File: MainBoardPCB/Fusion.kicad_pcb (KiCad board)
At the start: 4 copper layers, 91.5 x 52.1 mm, 140 parts, among them J1 Micro_SD_Card_Det_Hirose_DM3AT, J2 Conn_02x20_Odd_Even, J3 DX07S016JA1R1500, J4 Conn_02x07_Odd_Even, J5 Conn_02x16_Odd_Even, J7 Conn_02x08_Odd_Even, SW1 SW_Push, SW2 SW_Push, SW3 RESET, SW4 BOOT0, U1 STM32F723IETx, U2 TLV62568DDC, U3 MX25L3233FM1, U4 LFE5U-12-TG144, U5 NCP718xSN250, U6 USB6B1, U8 UGA, U9 TLV62568DDC, Y1 12MHz

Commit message: Fixes mistake in 1.0, FPGA boot cgf was forced into Master SPI mode
Just make it configurable with pull down resistors.

Signed-off-by: Alexis Jeandet <alexis.jeandet@member.fsf.org>
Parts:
- removed C55: 100nF, Capacitor_SMD:C_0402_1005Metric
- added R42: R, Resistor_SMD:R_0402_1005Metric_Pad0.72x0.64mm_HandSolder, B.Cu at (129.1, 79.7)
- added R43: R, Resistor_SMD:R_0402_1005Metric_Pad0.72x0.64mm_HandSolder, B.Cu at (130.2, 79.7)
- added R44: R, Resistor_SMD:R_0402_1005Metric_Pad0.72x0.64mm_HandSolder, B.Cu at (131.4, 79.7)
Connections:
- U4 pad 58: GND -> /FPGA/CFG_2
- U4 pad 59: /#3.3V -> /FPGA/CFG_1
- U4 pad 62: GND -> /FPGA/CFG_0
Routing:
- net /FPGA/CFG_2: track 0.00 -> 8.80 mm, vias 0 -> 1
- net /FPGA/CFG_1: track 0.00 -> 7.39 mm, vias 0 -> 1
- net /FPGA/CFG_0: track 0.00 -> 6.17 mm, vias 0 -> 1
- net /#3.3V: track 132.8 -> 130.9 mm, vias 42 -> 41
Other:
- board text added: "CFG0"
- board text added: "CFG1"
- board text added: "CFG2"

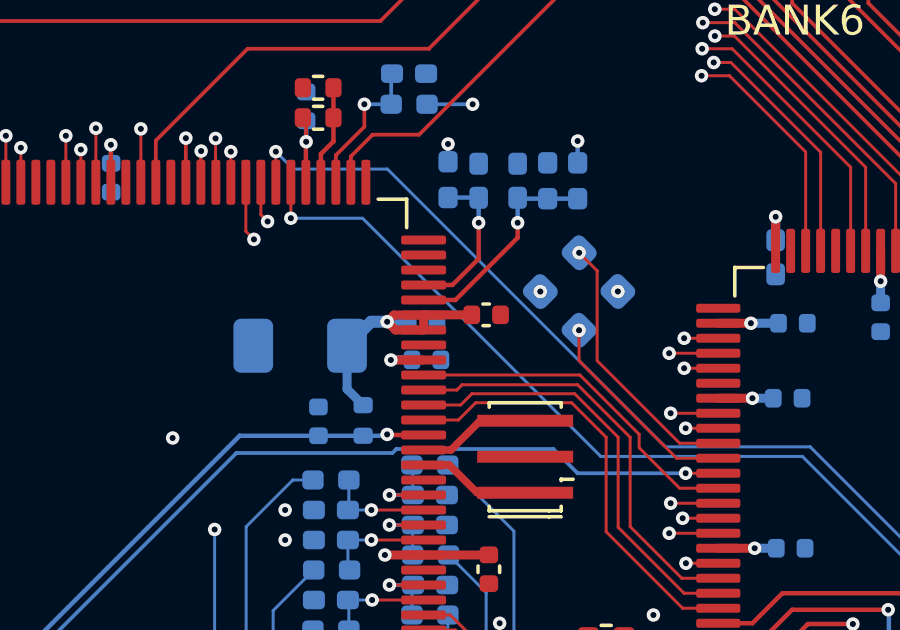
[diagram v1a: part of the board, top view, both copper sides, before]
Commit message: Fixes FPGA CFG slave serial interface wiring
Signed-off-by: Alexis Jeandet <alexis.jeandet@member.fsf.org>
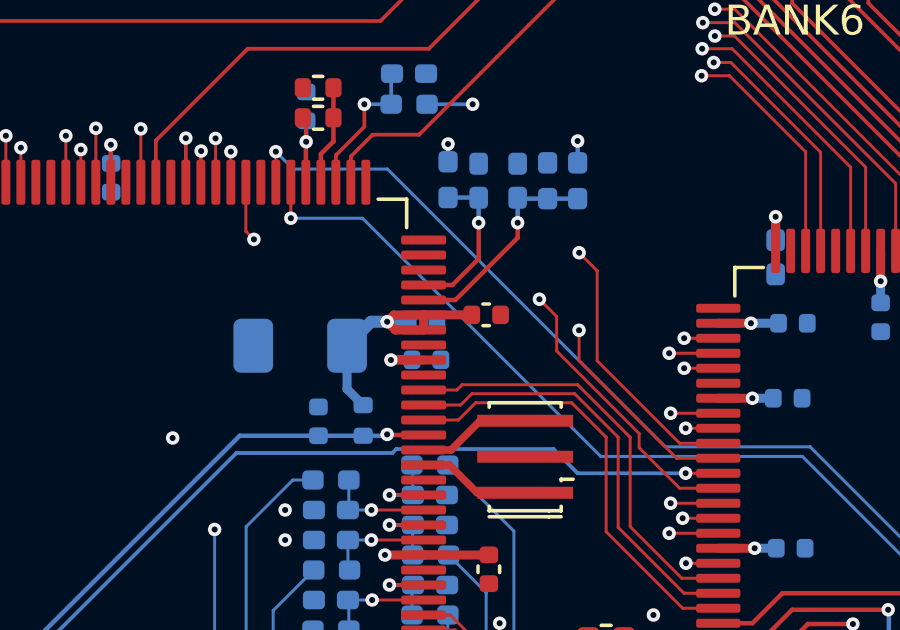
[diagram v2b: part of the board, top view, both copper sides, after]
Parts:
- removed U8: UGA, UGA:UGA_0603
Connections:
- U1 pad 35: /FPGA/FPGA_CFG_HOLDN -> /MCU/FPGA_CFG_HOLDN
- U1 pad 52: /FPGA/FPGA_CFG_MISO -> unconnected-(U1-PA6-Pad52)
- U4 pad 46: Net-(U4G-PB11A/+/D1/MISO/IO1) -> unconnected-(U4G-PB11A/+/D1/MISO/IO1-Pad46)
- U4 pad 47: Net-(U4G-PB11B/-/D0/MOSI/IO0) -> unconnected-(U4G-PB11B/-/D0/MOSI/IO0-Pad47)
- U4 pad 49: /FPGA/FPGA_CFG_HOLDN -> /FPGA/FPGA_CFG_MOSI
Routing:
- net /FPGA/FPGA_CFG_MISO: track 14.0 -> 0.00 mm, vias 2 -> 0
- net /FPGA/FPGA_CFG_HOLDN: track 11.6 -> 0.00 mm
- net /FPGA/FPGA_CFG_MOSI: track 12.3 -> 21.9 mm
- net unconnected-(U4G-PB11A/+/D1/MISO/IO1-Pad46): track 0.00 -> 9.03 mm, vias 0 -> 1
- net Net-(U4G-PB11A/+/D1/MISO/IO1): track 9.03 -> 0.00 mm, vias 1 -> 0
- net unconnected-(U4G-PB11B/-/D0/MOSI/IO0-Pad47): track 0.00 -> 7.00 mm, vias 0 -> 1
- net Net-(U4G-PB11B/-/D0/MOSI/IO0): track 7.00 -> 0.00 mm, vias 1 -> 0

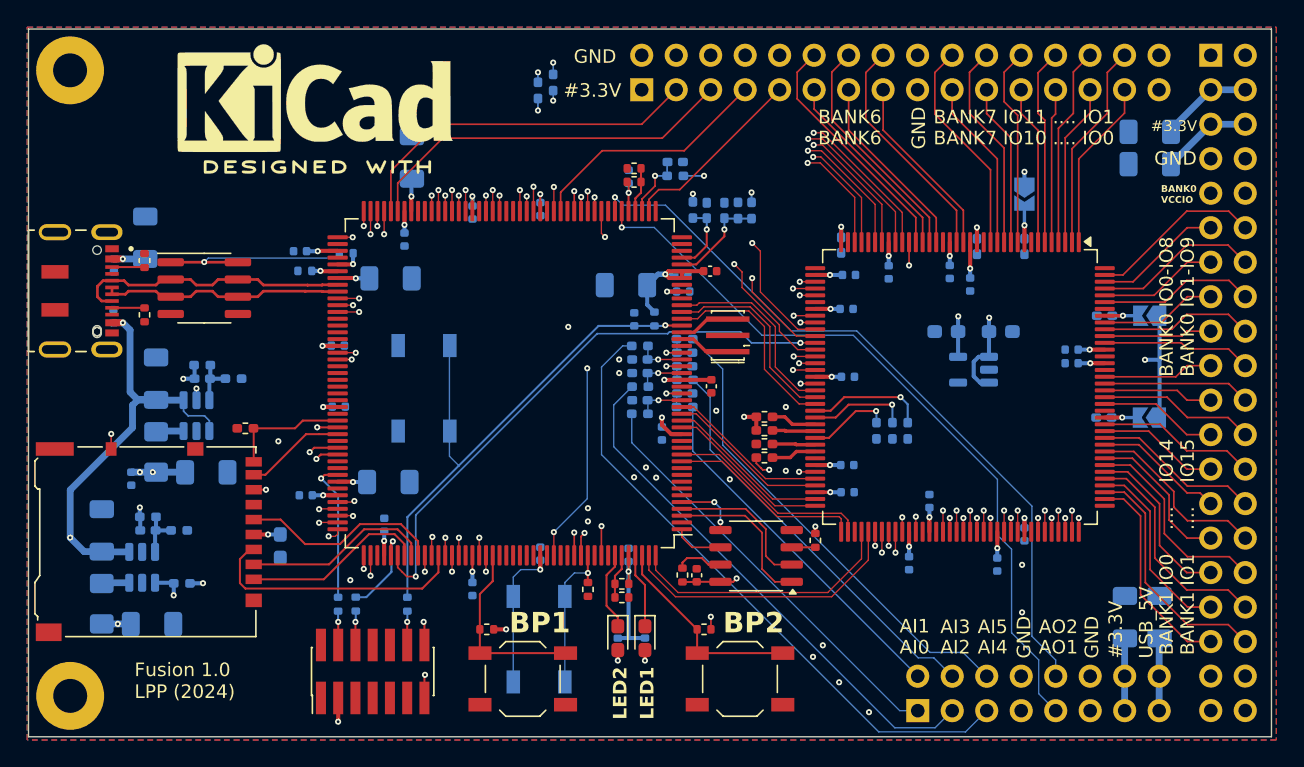
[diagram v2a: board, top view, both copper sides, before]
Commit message: New Fusion main board version using a more beefy MCU.
Signed-off-by: Alexis Jeandet <alexis.jeandet@member.fsf.org>
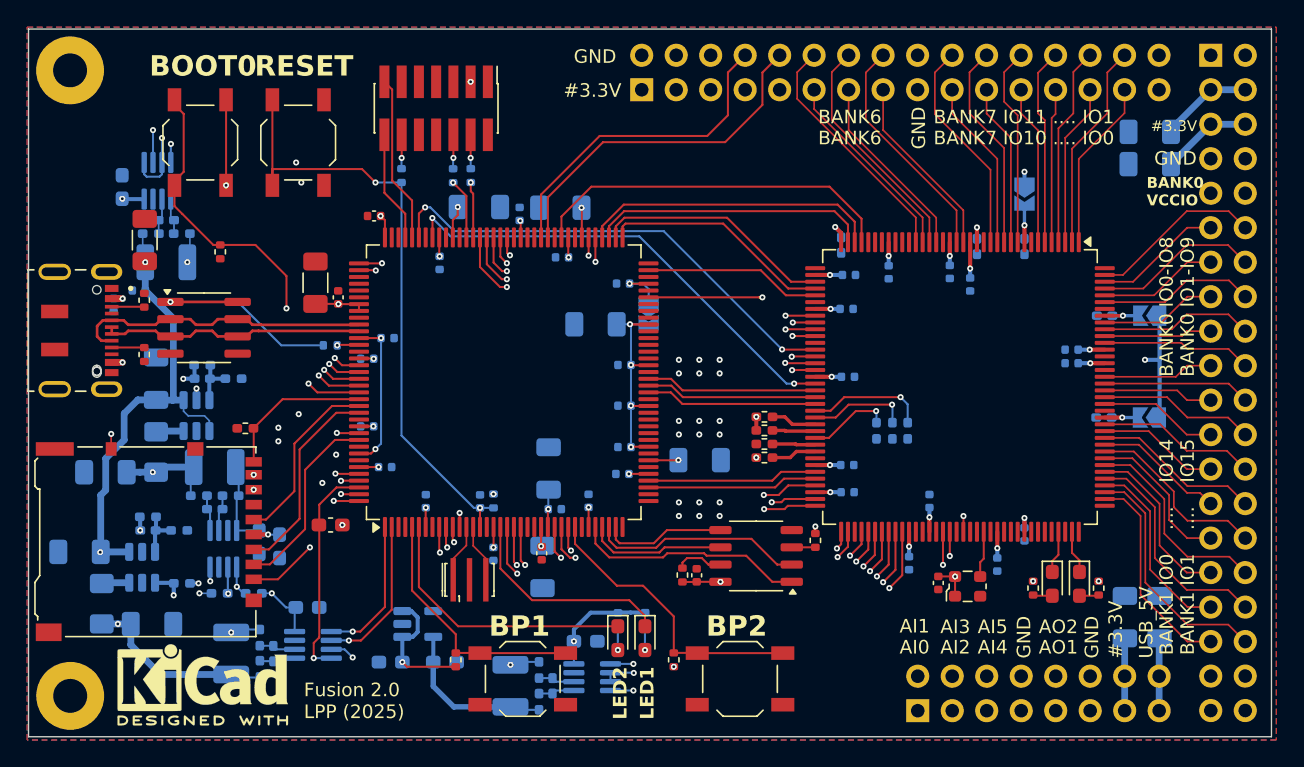
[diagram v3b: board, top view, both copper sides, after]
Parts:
- removed C13, C24, C25, C28, C29, C7: 100nF, Capacitor_SMD:C_0402_1005Metric
- removed C2, C21: 2.2µF, Capacitor_SMD:C_1206_3216Metric_Pad1.33x1.80mm_HandSolder
- removed C37, C41, C42, C43, C44, C45: 10nF, Capacitor_SMD:C_0402_1005Metric_Pad0.74x0.62mm_HandSolder
- removed C47, C48, C69: 100nF, Capacitor_SMD:C_0402_1005Metric_Pad0.74x0.62mm_HandSolder
- removed R10: 3K, Resistor_SMD:R_0402_1005Metric
- removed R15, R21, R22, R23, R24, R25: 1k, Resistor_SMD:R_0402_1005Metric_Pad0.72x0.64mm_HandSolder
- removed R19: 10k, Resistor_SMD:R_0402_1005Metric
- removed R35, R36, R37, R41: 10k, Resistor_SMD:R_0402_1005Metric_Pad0.72x0.64mm_HandSolder
- removed R5, R6, R7: 100k, Resistor_SMD:R_0402_1005Metric
- removed SYM1: Logo_Open_Hardware_Small, Symbol:OSHW-Logo_11.4x12mm_SilkScreen
- removed SYM2: Logo_Open_Hardware_Small, Symbol:KiCad-Logo2_8mm_SilkScreen
- removed U1: STM32F723IETx, Package_QFP:LQFP-176_24x24mm_P0.5mm
- added C1: 100nF, Capacitor_SMD:C_0402_1005Metric, F.Cu at (133.6, 90.9)
- added C1001: 100nF, Capacitor_SMD:C_0402_1005Metric_Pad0.74x0.62mm_HandSolder, B.Cu at (76.7, 64.2)
- added C1002: 100nF, Capacitor_SMD:C_0603_1608Metric_Pad1.08x0.95mm_HandSolder, B.Cu at (73.5, 61.8)
- added C217: 1µF, Capacitor_SMD:C_1206_3216Metric_Pad1.33x1.80mm_HandSolder, B.Cu at (104.5, 89.8)
- added C219: 100nF, Capacitor_SMD:C_0402_1005Metric, F.Cu at (104.4, 88.7)
- added C220: 100nF, Capacitor_SMD:C_0402_1005Metric, B.Cu at (93.0, 72.9)
- added C222: 2.2µF, Capacitor_SMD:C_1206_3216Metric_Pad1.33x1.80mm_HandSolder, B.Cu at (116.0, 81.9)
- added C223: 1µF, Capacitor_SMD:C_1206_3216Metric_Pad1.33x1.80mm_HandSolder, B.Cu at (104.9, 82.5)
- added C224: 100nF, Capacitor_SMD:C_0402_1005Metric, B.Cu at (105.4, 85.5)
- added C225: 1µF, Capacitor_SMD:C_1206_3216Metric_Pad1.33x1.80mm_HandSolder, F.Cu at (87.7, 68.8)
- added C226: 100nF, Capacitor_SMD:C_0402_1005Metric, F.Cu at (89.4, 69.9)
- added C227: 1µF, Capacitor_SMD:C_1206_3216Metric_Pad1.33x1.80mm_HandSolder, B.Cu at (108.4, 71.9)
- added C228: 100nF, Capacitor_SMD:C_0402_1005Metric, B.Cu at (110.5, 80.9)
- added C229: 100nF, Capacitor_SMD:C_0402_1005Metric, B.Cu at (110.5, 77.9)
- added C230: 100nF, Capacitor_SMD:C_0402_1005Metric, B.Cu at (110.5, 74.9)
- added C501: 100nF, Capacitor_SMD:C_0402_1005Metric_Pad0.74x0.62mm_HandSolder, B.Cu at (80.3, 85.5)
- added C502: 100nF, Capacitor_SMD:C_0603_1608Metric_Pad1.08x0.95mm_HandSolder, B.Cu at (83.6, 87.9)
- added C801: 100nF, Capacitor_SMD:C_0402_1005Metric_Pad0.74x0.62mm_HandSolder, B.Cu at (84.6, 96.1)
- added C802: 100nF, Capacitor_SMD:C_0603_1608Metric_Pad1.08x0.95mm_HandSolder, B.Cu at (87.1, 92.7)
- added C901: 100nF, Capacitor_SMD:C_0402_1005Metric_Pad0.74x0.62mm_HandSolder, B.Cu at (105.2, 98.5)
- added C902: 100nF, Capacitor_SMD:C_0603_1608Metric_Pad1.08x0.95mm_HandSolder, B.Cu at (107.6, 95.2)
- added D301: LED, LED_SMD:LED_0603_1608Metric_Pad1.05x0.95mm_HandSolder, F.Cu at (142.0, 91.0)
- added D302: LED, LED_SMD:LED_0603_1608Metric_Pad1.05x0.95mm_HandSolder, F.Cu at (144.0, 91.0)
- added JP201: SolderJumper_2_Open, Jumper:SolderJumper-2_P1.3mm_Open_TrianglePad1.0x1.5mm, B.Cu at (112.3, 71.1)
- added R1001: R, Resistor_SMD:R_1210_3225Metric_Pad1.30x2.65mm_HandSolder, B.Cu at (76.7, 67.3)
- added R1002: 100, Resistor_SMD:R_0402_1005Metric_Pad0.72x0.64mm_HandSolder, B.Cu at (77.9, 65.2)
- added R1003: 100, Resistor_SMD:R_0402_1005Metric_Pad0.72x0.64mm_HandSolder, B.Cu at (75.6, 65.2)
- added R101: 10k, Capacitor_SMD:C_0603_1608Metric_Pad1.08x0.95mm_HandSolder, F.Cu at (88.8, 86.7)
- added R308: 2.2k, Resistor_SMD:R_0402_1005Metric, F.Cu at (140.6, 91.3)
- added R309: 2.2k, Resistor_SMD:R_0402_1005Metric, F.Cu at (145.4, 91.3)
- added R501: R, Resistor_SMD:R_1210_3225Metric_Pad1.30x2.65mm_HandSolder, B.Cu at (80.3, 82.4)
- added R502: 100, Resistor_SMD:R_0402_1005Metric_Pad0.72x0.64mm_HandSolder, B.Cu at (79.1, 84.5)
- added R503: 100, Resistor_SMD:R_0402_1005Metric_Pad0.72x0.64mm_HandSolder, B.Cu at (81.5, 84.5)
- added R801: R, Resistor_SMD:R_1210_3225Metric_Pad1.30x2.65mm_HandSolder, B.Cu at (81.5, 96.1)
- added R802: 100, Resistor_SMD:R_0402_1005Metric_Pad0.72x0.64mm_HandSolder, B.Cu at (83.6, 97.3)
- added R803: 100, Resistor_SMD:R_0402_1005Metric_Pad0.72x0.64mm_HandSolder, B.Cu at (83.6, 95.0)
- added R901: R, Resistor_SMD:R_1210_3225Metric_Pad1.30x2.65mm_HandSolder, B.Cu at (102.1, 98.5)
- added R902: 100, Resistor_SMD:R_0402_1005Metric_Pad0.72x0.64mm_HandSolder, B.Cu at (104.2, 99.7)
- added R903: 100, Resistor_SMD:R_0402_1005Metric_Pad0.72x0.64mm_HandSolder, B.Cu at (104.2, 97.3)
- added REF**: KiCad-Logo2_5mm_SilkScreen, Symbol:KiCad-Logo2_5mm_SilkScreen, F.Cu at (79.4, 98.4)
- added SYM101: Logo_Open_Hardware_Small, Symbol:OSHW-Logo_11.4x12mm_SilkScreen, B.Cu at (120.6, 95.4)
- added U1001: INA236, Package_TO_SOT_SMD:SOT-23-8_Handsoldering, B.Cu at (76.1, 61.3)
- added U203: STM32H7S3Z8Tx, Package_QFP:LQFP-144_20x20mm_P0.5mm, F.Cu at (101.6, 76.1)
- added U501: INA236, Package_TO_SOT_SMD:SOT-23-8_Handsoldering, B.Cu at (80.9, 88.4)
- added U801: INA236, Package_TO_SOT_SMD:SOT-23-8_Handsoldering, B.Cu at (87.5, 95.5)
- added U901: INA236, Package_TO_SOT_SMD:SOT-23-8_Handsoldering, B.Cu at (108.1, 97.9)
- added X1: ECS-2520MV-xxx-xx, Oscillator:Oscillator_SMD_ECS_2520MV-xxx-xx-4Pin_2.5x2.0mm, F.Cu at (135.8, 91.2)
- C207: renamed from C15; moved to B.Cu
- C211: renamed from C17; moved to F.Cu
- C402: renamed from C8; value 10µF -> 100nF; footprint Capacitor_SMD:C_1206_3216Metric_Pad1.33x1.80mm_HandSolder -> Capacitor_SMD:C_0402_1005Metric
- C403: renamed from C10; value 100nF -> 10µF; footprint Capacitor_SMD:C_0402_1005Metric -> Capacitor_SMD:C_1206_3216Metric_Pad1.33x1.80mm_HandSolder; moved to F.Cu
- SW203: renamed from SW4; moved to F.Cu
- SW204: renamed from SW3; moved to F.Cu
- moved C401 51.1 mm to (93.3, 96.8), turned to 180 degrees
- moved U401 45.0 mm to (95.3, 94.0), turned to 0 degrees
- moved SW203 44.3 mm to (79.2, 58.5)
- moved C404 44.2 mm to (97.3, 96.8), turned to 0 degrees
- moved R216 43.8 mm to (80.7, 91.7), turned to 180 degrees
- moved R217 43.6 mm to (83.2, 91.7), turned to 0 degrees
- moved J201 41.7 mm to (96.6, 56.0), turned to -90 degrees
- moved R215 36.8 mm to (80.7, 66.5)
- moved C212 33.7 mm to (107.8, 84.9), turned to 90 degrees
- moved R203 33.0 mm to (99.2, 60.9), turned to -90 degrees
- moved R204 32.4 mm to (97.9, 60.9), turned to -90 degrees
- moved R205 31.6 mm to (94.1, 60.9), turned to -90 degrees
- moved C211 27.7 mm to (92.0, 63.9), turned to 180 degrees
- moved C208 26.4 mm to (102.8, 63.8)
- moved Y201 26.2 mm to (99.1, 90.7), turned to 0 degrees
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- renumbered C49 to C101, C19 to C102, C50 to C103, C20 to C104, C3 to C201, C4 to C202, C51 to C203, C26 to C204, C27 to C205, C9 to C206, C16 to C208, C11 to C209, C12 to C210, C22 to C212, C30 to C213, C1 to C214, C46 to C215, C14 to C216, C18 to C218, C23 to C221, C65 to C301, C66 to C302, C67 to C303, C68 to C304, C59 to C305, C60 to C306, C61 to C307, C62 to C308, C5 to C309, C63 to C310, C64 to C311, C31 to C312, C54 to C313, C33 to C314, C56 to C315, C57 to C316, C35 to C317, C58 to C318, C36 to C319, C52 to C401, C53 to C404, C6 to C601, C32 to C602, C34 to C603, C38 to C701, C39 to C702, C40 to C703, D1 to D201, D2 to D202, H1 to H101, H2 to H102, J7 to J101, J5 to J102, J2 to J103, J4 to J201, J1 to J202, J3 to J203, JP1 to JP101, JP2 to JP102, JP3 to JP103, L2 to L601, L3 to L701, R16 to R201, R4 to R202, R1 to R203, R2 to R204, R3 to R205, R14 to R206, R20 to R207, R38 to R208, R12 to R209, R13 to R210, R17 to R211, R18 to R212, R11 to R213, R8 to R214, R9 to R215, R39 to R216, R40 to R217, R26 to R301, R27 to R302, R28 to R303, R29 to R304, R42 to R305, R43 to R306, R44 to R307, R34 to R401, R31 to R601, R32 to R602, R30 to R701, R33 to R702, SW1 to SW201, SW2 to SW202, U3 to U201, U6 to U202, U4 to U301, U5 to U401, U2 to U601, U9 to U701, Y1 to Y201
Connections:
- C103 pad 1: /USB_5V -> /5V
- C104 pad 1: /USB_5V -> /5V
- C218 pad 1: Net-(U1-V12PHYHS) -> /MCU/VCap
- C221 pad 1: /#3.3V -> /MCU/VCap
- C402 pad 1: /USB_5V -> /5V
- C403 pad 1: /USB_5V -> /5V
- C404 pad 1: /#2.5V -> /Power/PowerMonitor2/Vin
- C601 pad 1: /USB_5V -> /5V
- C602 pad 1: /#3.3V -> /Power/PowerMonitor1/Vin
- C603 pad 1: /#3.3V -> /Power/PowerMonitor1/Vin
- C701 pad 1: /USB_5V -> /5V
- C702 pad 1: /#1.1V -> /Power/PowerMonitor/Vin
- C703 pad 1: /#1.1V -> /Power/PowerMonitor/Vin
- J101 pad 15: /USB_5V -> /5V
- J101 pad 16: /USB_5V -> /5V
- J103 pad 3: /USB_5V -> /5V
- J103 pad 4: /USB_5V -> /5V
- L601 pad 2: /#3.3V -> /Power/PowerMonitor1/Vin
- L701 pad 2: /#1.1V -> /Power/PowerMonitor/Vin
- R213 pad 1: Net-(U1-PB13) -> /MCU/VBUS_SENSE
- R601 pad 1: /#3.3V -> /Power/PowerMonitor1/Vin
- R701 pad 1: /#1.1V -> /Power/PowerMonitor/Vin
- U301 pad 102: /FPGA/FPGA_D13 -> unconnected-(U301C-PR8D/-/RDQ8-Pad102)
- U301 pad 103: /FPGA/FPGA_D20 -> unconnected-(U301C-PR8B/-/HS/RDQSN8-Pad103)
- U301 pad 104: /FPGA/FPGA_D19 -> unconnected-(U301C-PR8C/+/RDQ8-Pad104)
- U301 pad 105: /FPGA/FPGA_D18 -> /FPGA/LED1
- U301 pad 106: /FPGA/FPGA_D17 -> unconnected-(U301C-PR2D/-/RDQ8-Pad106)
- U301 pad 107: /FPGA/FPGA_D16 -> /FPGA/LED2
- U301 pad 108: /FPGA/FPGA_D12 -> unconnected-(U301C-PR2B/-/HS/RDQ8/S0_IN-Pad108)
- U301 pad 26: /FPGA/FPGA_NL -> unconnected-(U301E-PL41C/+/LDQ44-Pad26)
- U301 pad 27: /FPGA/FPGA_IO5 -> unconnected-(U301E-PL41D/-/LDQ44-Pad27)
- U301 pad 28: /FPGA/FPGA_IO4 -> unconnected-(U301E-PL44A/+/HS/LDQS44-Pad28)
- U301 pad 30: /FPGA/FPGA_IO3 -> unconnected-(U301E-PL44B/-/HS/LDQSN44-Pad30)
- U301 pad 31: /FPGA/FPGA_IO2 -> unconnected-(U301E-PL44C/+/LDQ44-Pad31)
- U301 pad 33: /FPGA/FPGA_IO1 -> /FPGA/FPGA_HAVE_DATA
- U301 pad 34: /FPGA/FPGA_IO0 -> /FPGA/FPGA_D8
- U301 pad 35: unconnected-(U4E-PL47B/-/HS/LDQ44-Pad35) -> /FPGA/FPGA_D9
- U301 pad 39: /FPGA/FPGA_D4 -> /FPGA/FPGA_D10
- U301 pad 40: /FPGA/FPGA_D5 -> /FPGA/FPGA_D11
- U301 pad 41: /FPGA/FPGA_D6 -> /FPGA/FPGA_NE1
- U301 pad 44: /FPGA/FPGA_D7 -> /FPGA/FPGA_D4
- U301 pad 45: /FPGA/FPGA_D8 -> /FPGA/FPGA_D3
- U301 pad 46: unconnected-(U4G-PB11A/+/D1/MISO/IO1-Pad46) -> /FPGA/FPGA_D2
- U301 pad 47: unconnected-(U4G-PB11B/-/D0/MOSI/IO0-Pad47) -> /FPGA/FPGA_D1
- U301 pad 48: /FPGA/FPGA_CFG_CS -> unconnected-(U301G-PB13A/+/SN/CSN-Pad48)
- U301 pad 50: /FPGA/FPGA_D9 -> /FPGA/FPGA_D0
- U301 pad 51: /FPGA/FPGA_D10 -> /FPGA/FPGA_NWAIT
- U301 pad 52: /FPGA/FPGA_D11 -> /FPGA/FPGA_NL
- U301 pad 67: /FPGA/FPGA_NWAIT -> /FPGA/FPGA_NWE
- U301 pad 68: /FPGA/FPGA_HAVE_DATA -> /FPGA/FPGA_NOE
- U301 pad 69: /FPGA/FPGA_A2 -> /FPGA/FPGA_D5
- U301 pad 71: /FPGA/FPGA_A1 -> /FPGA/FPGA_D6
- U301 pad 72: /FPGA/FPGA_A0 -> /FPGA/FPGA_D7
- U301 pad 73: /FPGA/FPGA_D30 -> /FPGA/FPGA_A2
- U301 pad 74: /FPGA/FPGA_D31 -> /FPGA/FPGA_A1
- U301 pad 76: /FPGA/FPGA_D29 -> /FPGA/FPGA_A0
- U301 pad 77: /FPGA/FPGA_D28 -> /FPGA/FPGA_D15
- U301 pad 78: /FPGA/FPGA_D26 -> /FPGA/FPGA_D14
- U301 pad 79: /FPGA/FPGA_D27 -> /FPGA/FPGA_D13
- U301 pad 80: /FPGA/FPGA_D25 -> /FPGA/FPGA_D12
- U301 pad 81: /FPGA/FPGA_D24 -> /FPGA/FPGA_UART_TX
- U301 pad 82: /FPGA/FPGA_D23 -> /FPGA/FPGA_UART_RX
- U301 pad 84: /FPGA/FPGA_D22 -> unconnected-(U301D-PR32C/+/RDQ32-Pad84)
- U301 pad 88: /FPGA/FPGA_D21 -> /FPGA/FPGA_UART2_RX
- U301 pad 89: /FPGA/FPGA_NE1 -> /FPGA/FPGA_UART2_TX
- U301 pad 90: /FPGA/FPGA_NOE -> unconnected-(U301C-PR23C/+/RDQ20/PCLKT2_0-Pad90)
- U301 pad 91: /FPGA/FPGA_D2 -> /FPGA/FPGA_CLK
- U301 pad 92: /FPGA/FPGA_D3 -> unconnected-(U301C-PR20D/-/RDQ20-Pad92)
- U301 pad 93: /FPGA/FPGA_CLK -> unconnected-(U301C-PR20B/-/HS/RDQSN20-Pad93)
- U301 pad 94: /FPGA/FPGA_NWE -> /FPGA/FPGA_OPT_CLK
- U301 pad 95: /FPGA/FPGA_D1 -> unconnected-(U301C-PR20A/+/HS/RDQS20/GR_PCLK2_1-Pad95)
- U301 pad 97: /FPGA/FPGA_D0 -> unconnected-(U301C-PR14B/-/HS/RDQ20-Pad97)
- U301 pad 98: /FPGA/FPGA_D15 -> unconnected-(U301C-PR14C/+/RDQ20/VREF1_2-Pad98)
- U301 pad 99: /FPGA/FPGA_D14 -> unconnected-(U301C-PR14A/+/HS/RDQ20-Pad99)
- U401 pad 5: /#2.5V -> /Power/PowerMonitor2/Vin
- U601 pad 1: /USB_5V -> /5V
- U601 pad 4: /USB_5V -> /5V
- U701 pad 4: /USB_5V -> /5V
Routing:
- net /5V: track 0.00 -> 181.1 mm, vias 0 -> 2
- net /USB_5V: track 211.2 -> 34.4 mm
- net /Alert: track 0.00 -> 88.7 mm, vias 0 -> 4
- net /FPGA/FPGA_D18: track 63.0 -> 0.00 mm, vias 2 -> 0
- net /FPGA/FPGA_D17: track 63.0 -> 0.00 mm, vias 2 -> 0
- net /FPGA/FPGA_D16: track 63.0 -> 0.00 mm, vias 2 -> 0
- net /FPGA/FPGA_D19: track 63.0 -> 0.00 mm, vias 2 -> 0
- net /FPGA/FPGA_D20: track 62.2 -> 0.00 mm, vias 2 -> 0
- net /MCU/VCap: track 0.00 -> 61.9 mm, vias 0 -> 5
- net /FPGA/FPGA_UART2_TX: track 0.00 -> 57.2 mm, vias 0 -> 2
- net /FPGA/FPGA_UART2_RX: track 0.00 -> 55.4 mm, vias 0 -> 2
- net /DAC_OUT1: track 55.4 -> 0.00 mm, vias 1 -> 0
- net /DAC_OUT2: track 54.4 -> 0.00 mm, vias 1 -> 0
- net /FPGA/FPGA_D22: track 52.7 -> 0.00 mm, vias 2 -> 0
- net /FPGA/FPGA_UART_TX: track 0.00 -> 52.7 mm, vias 0 -> 2
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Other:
- board text added: "Fusion 2.0 LPP (2025)"
- board text removed: "Fusion 1.0 LPP (2024)"

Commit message: New FPGA only version
Signed-off-by: Alexis Jeandet <alexis.jeandet@member.fsf.org>
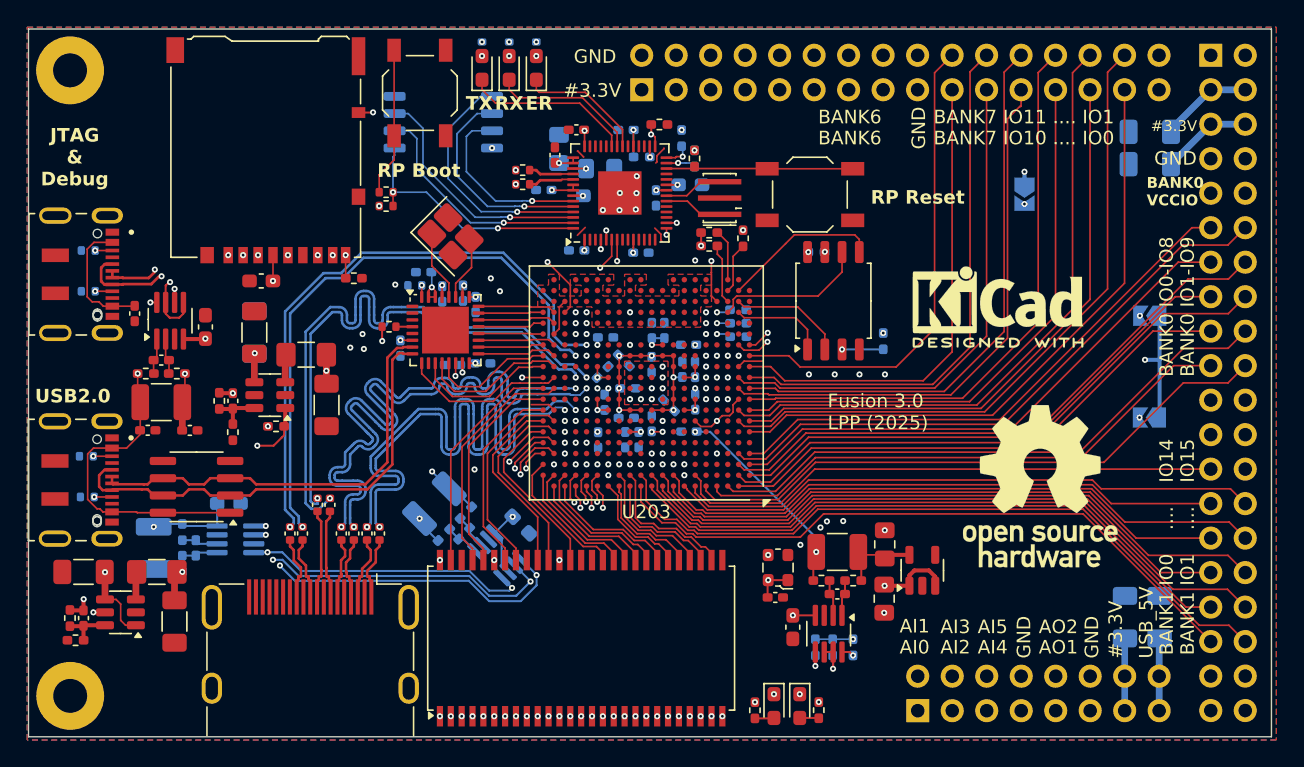
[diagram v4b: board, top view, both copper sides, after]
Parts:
- removed C209, C210, C211, C212, C213, C216, C219, C220, C224, C226, C228, C229, C230: 100nF, Capacitor_SMD:C_0402_1005Metric
- removed C214: 100nF, Capacitor_SMD:C_0603_1608Metric_Pad1.08x0.95mm_HandSolder
- removed C217, C223, C225, C227: 1µF, Capacitor_SMD:C_1206_3216Metric_Pad1.33x1.80mm_HandSolder
- removed C218, C221, C222: 2.2µF, Capacitor_SMD:C_1206_3216Metric_Pad1.33x1.80mm_HandSolder
- removed D201, D202: LED, LED_SMD:LED_0603_1608Metric_Pad1.05x0.95mm_HandSolder
- removed JP201: SolderJumper_2_Open, Jumper:SolderJumper-2_P1.3mm_Open_TrianglePad1.0x1.5mm
- removed R206, R214, R215: 100k, Resistor_SMD:R_0402_1005Metric
- removed R207, R208, R209, R210: 2.2k, Resistor_SMD:R_0402_1005Metric
- removed R216, R217: 10k, Resistor_SMD:R_0402_1005Metric_Pad0.72x0.64mm_HandSolder
- removed SW202: SW_Push, Button_Switch_SMD:SW_SPST_TL3342
- removed SW203: BOOT0, Button_Switch_SMD:SW_SPST_TL3342
- removed SW204: RESET, Button_Switch_SMD:SW_SPST_TL3342
- removed U201: MX25L3233FM1, Package_SO:SOP-8_3.9x4.9mm_P1.27mm
- removed U301: LFE5U-12-TG144, Package_QFP:TQFP-144_20x20mm_P0.5mm
- added C1003: 100nF, Capacitor_SMD:C_0402_1005Metric_Pad0.74x0.62mm_HandSolder, B.Cu at (97.1, 69.7)
- added C1004: 100nF, Capacitor_SMD:C_0402_1005Metric_Pad0.74x0.62mm_HandSolder, B.Cu at (97.8, 74.9)
- added C1005: 100nF, Capacitor_SMD:C_0402_1005Metric_Pad0.74x0.62mm_HandSolder, B.Cu at (98.6, 69.6)
- added C1006: 100nF, Capacitor_SMD:C_0402_1005Metric_Pad0.74x0.62mm_HandSolder, B.Cu at (94.0, 73.6)
- added C1007: 100nF, Capacitor_SMD:C_0402_1005Metric_Pad0.74x0.62mm_HandSolder, B.Cu at (100.0, 74.8)
- added C1008: 100nF, Capacitor_SMD:C_0402_1005Metric_Pad0.74x0.62mm_HandSolder, B.Cu at (99.5, 70.4)
- added C1009: 100nF, Capacitor_SMD:C_0402_1005Metric_Pad0.74x0.62mm_HandSolder, B.Cu at (95.7, 68.0)
- added C115: 100nF, Capacitor_SMD:C_0603_1608Metric_Pad1.08x0.95mm_HandSolder, F.Cu at (83.7, 68.7)
- added C1201: 100nF, Capacitor_SMD:C_0402_1005Metric_Pad0.74x0.62mm_HandSolder, F.Cu at (74.4, 71.1)
- added C1202: 100nF, Capacitor_SMD:C_0402_1005Metric_Pad0.74x0.62mm_HandSolder, B.Cu at (112.8, 62.6)
- added C1203: 1uF, Capacitor_SMD:C_0805_2012Metric_Pad1.18x1.45mm_HandSolder, B.Cu at (108.7, 60.4)
- added C1204: 100nF, Capacitor_SMD:C_0603_1608Metric_Pad1.08x0.95mm_HandSolder, B.Cu at (108.3, 62.4)
- added C1205: 100nF, Capacitor_SMD:C_0603_1608Metric_Pad1.08x0.95mm_HandSolder, B.Cu at (115.3, 61.6)
- added C1206: 100nF, Capacitor_SMD:C_0402_1005Metric_Pad0.74x0.62mm_HandSolder, B.Cu at (111.7, 66.6)
- added C1207: 100nF, Capacitor_SMD:C_0402_1005Metric_Pad0.74x0.62mm_HandSolder, B.Cu at (107.0, 66.4)
- added C1208: 1uF, Capacitor_SMD:C_0805_2012Metric_Pad1.18x1.45mm_HandSolder, B.Cu at (105.7, 59.0)
- added C1209: 100nF, Capacitor_SMD:C_0402_1005Metric_Pad0.74x0.62mm_HandSolder, B.Cu at (110.6, 57.6)
- added C1210: 100nF, Capacitor_SMD:C_0402_1005Metric_Pad0.74x0.62mm_HandSolder, F.Cu at (107.0, 57.6)
- added C1211: 100nF, Capacitor_SMD:C_0402_1005Metric_Pad0.74x0.62mm_HandSolder, B.Cu at (104.5, 62.0)
- added C1212: 100nF, Capacitor_SMD:C_0402_1005Metric_Pad0.74x0.62mm_HandSolder, F.Cu at (105.4, 59.4)
- added D1201: LED, LED_SMD:LED_0603_1608Metric_Pad1.05x0.95mm_HandSolder, F.Cu at (100.0, 53.0)
- added D1202: LED, LED_SMD:LED_0603_1608Metric_Pad1.05x0.95mm_HandSolder, F.Cu at (102.0, 53.0)
- added D1203: LED, LED_SMD:LED_0603_1608Metric_Pad1.05x0.95mm_HandSolder, F.Cu at (104.0, 53.0)
- added J1201: DX07S016JA1R1500, DX07S016JA1R1500:JAE_DX07S016JA1R1500, F.Cu at (71.7, 68.2)
- added R1004: 12k, Resistor_SMD:R_0402_1005Metric, B.Cu at (95.1, 69.0)
- added R108: 10k, Resistor_SMD:R_0402_1005Metric_Pad0.72x0.64mm_HandSolder, F.Cu at (90.6, 68.5)
- added R1201: 5.1k, Resistor_SMD:R_0402_1005Metric, B.Cu at (71.0, 66.5)
- added R1202: 5.1k, Resistor_SMD:R_0402_1005Metric, B.Cu at (71.0, 69.5)
- added R1203: 2.2k, Resistor_SMD:R_0402_1005Metric, B.Cu at (100.0, 51.6)
- added R1204: 27, Resistor_SMD:R_0402_1005Metric, F.Cu at (103.0, 60.5)
- added R1205: 27, Resistor_SMD:R_0402_1005Metric, F.Cu at (103.0, 61.6)
- added R1206: 1k, Resistor_SMD:R_0402_1005Metric, F.Cu at (92.9, 62.2)
- added R1207: 1k, Resistor_SMD:R_0402_1005Metric, F.Cu at (92.9, 63.2)
- added R1208: 10k, Resistor_SMD:R_0402_1005Metric_Pad0.72x0.64mm_HandSolder, F.Cu at (115.7, 59.7)
- added R1209: 2.2k, Resistor_SMD:R_0402_1005Metric, B.Cu at (102.0, 51.6)
- added R1210: 2.2k, Resistor_SMD:R_0402_1005Metric, B.Cu at (104.0, 51.6)
- added R1211: 4.7k, Resistor_SMD:R_0402_1005Metric_Pad0.72x0.64mm_HandSolder, B.Cu at (125.8, 95.7)
- added R1212: 4.7k, Resistor_SMD:R_0402_1005Metric_Pad0.72x0.64mm_HandSolder, B.Cu at (124.5, 95.7)
- added SW1201: SW_Push, Button_Switch_SMD:SW_SPST_TL3342, F.Cu at (124.2, 62.3)
- added U10: IS25LP128F-JBLE, Package_SO:SOIC-8_5.3x5.3mm_P1.27mm, F.Cu at (125.9, 70.2)
- added U1002: USB3300-EZK, Package_DFN_QFN:QFN-32-1EP_5x5mm_P0.5mm_EP3.45x3.45mm, F.Cu at (97.3, 72.3)
- added U1101: MT48LC16M16A2P, Package_SO:TSOP-II-54_22.2x10.16mm_P0.8mm, F.Cu at (107.3, 95.0)
- added U1201: RP2040, Package_DFN_QFN:QFN-56-1EP_7x7mm_P0.4mm_EP3.2x3.2mm, F.Cu at (110.2, 62.2)
- added U1203: W25Q16JVSS, Package_SO:SOIC-8_5.3x5.3mm_P1.27mm, B.Cu at (97.2, 57.0)
- added Y1001: Crystal_GND24_Small, Crystal:Crystal_SMD_EuroQuartz_X22-4Pin_2.5x2.0mm_HandSoldering, F.Cu at (97.7, 65.4)
- C1, C301, C302, C303, C304, C305, C306, C307, C308, C310, C311, C313, C315, C316, C318: footprint Capacitor_SMD:C_0402_1005Metric -> Capacitor_SMD:C_0402_1005Metric_Pad0.74x0.62mm_HandSolder
- C1001, C1002, C601, C602, C603, C701, C702, C703, C901, C902, L601, L701, R1001, R1002, R1003, R213, R601, R602, R701, R702, R901, R902, R903, SYM101, U1001, U401, U601, U701, U901: moved to F.Cu
- C201, C202, C204, C205, C206, C207, C208: value 100nF -> 22nF; moved to F.Cu
- C203: value 100nF -> 22nF
- C215, C402: footprint Capacitor_SMD:C_0402_1005Metric -> Capacitor_SMD:C_0402_1005Metric_Pad0.74x0.62mm_HandSolder; moved to F.Cu
- C401, C404: footprint Capacitor_SMD:C_0603_1608Metric_Pad1.08x0.95mm_HandSolder -> Capacitor_SMD:C_0805_2012Metric_Pad1.18x1.45mm_HandSolder; moved to F.Cu
- C403, R202, R211, R212, R301, R303, R304: moved to B.Cu
- J201: value Conn_02x07_Odd_Even -> HDMI_A; footprint Connector_PinHeader_1.27mm:PinHeader_2x07_P1.27mm_Vertical_SMD -> Connector_Video:HDMI_A_Molex_208658-1001_Horizontal
- R101: footprint Capacitor_SMD:C_0603_1608Metric_Pad1.08x0.95mm_HandSolder -> Resistor_SMD:R_0402_1005Metric_Pad0.72x0.64mm_HandSolder; moved to B.Cu
- R201: value 100k -> 10k; footprint Resistor_SMD:R_0402_1005Metric -> Resistor_SMD:R_0402_1005Metric_Pad0.72x0.64mm_HandSolder; moved to B.Cu
- R203, R204, R205: value 22 -> 10k; footprint Resistor_SMD:R_0402_1005Metric -> Resistor_SMD:R_0402_1005Metric_Pad0.72x0.64mm_HandSolder; moved to F.Cu
- R305, R306, R307: value R -> 0
- R308, R309: footprint Resistor_SMD:R_0402_1005Metric -> Resistor_SMD:R_0402_1005Metric_Pad0.72x0.64mm_HandSolder
- R401: value R -> 100k; moved to F.Cu
- U203: value STM32H7S3Z8Tx -> LFE5U-85F-6BG381x; footprint Package_QFP:LQFP-144_20x20mm_P0.5mm -> Package_BGA:Lattice_caBGA-381_17x17mm_Layout20x20_P0.8mm
- moved REF** 64.8 mm to (138.0, 70.6)
- moved R202 44.0 mm to (124.6, 66.6)
- moved SW201 43.8 mm to (95.4, 54.9), turned to 90 degrees
- moved J201 40.4 mm to (87.3, 95.2)
- moved R101 39.5 mm to (127.3, 95.7), turned to -90 degrees
- moved R201 39.3 mm to (129.6, 73.1), turned to -90 degrees
- moved U401 37.4 mm to (132.4, 90.0), turned to 90 degrees
- moved C401 36.6 mm to (129.6, 92.1), turned to -90 degrees
- moved C302 35.5 mm to (108.5, 80.4), turned to -90 degrees
- moved Y201 33.6 mm to (117.5, 62.6), turned to 90 degrees
- moved C404 33.5 mm to (129.7, 88.1), turned to 90 degrees
- moved C304 33.3 mm to (109.1, 72.8), turned to 0 degrees
- moved C309 33.3 mm to (112.5, 79.2), turned to 90 degrees
- moved C310 33.0 mm to (110.6, 78.8), turned to 0 degrees
- moved C318 31.3 mm to (112.5, 72.3), turned to 90 degrees
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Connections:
- net /5V renamed /FPGA/5V
- C1 pad 1: /#3.3V -> /FPGA/3.3V
- C1002 pad 1: /#3.3V -> /FPGA/3.3V
- C101 pad 1: /#3.3V -> /FPGA/3.3V
- C102 pad 1: /#3.3V -> /FPGA/3.3V
- C201 pad 1: /#3.3V -> /FPGA/HDMI_D2+
- C201 pad 2: GND -> /FPGA/_HDMI_D2+
- C202 pad 1: /#3.3V -> /FPGA/HDMI_D2-
- C202 pad 2: GND -> /FPGA/_HDMI_D2-
- C203 pad 1: /#3.3V -> /FPGA/HDMI_D1-
- C203 pad 2: GND -> /FPGA/_HDMI_D1-
- C204 pad 1: /#3.3V -> /FPGA/HDMI_D1+
- C204 pad 2: GND -> /FPGA/_HDMI_D1+
- C205 pad 1: /#3.3V -> /FPGA/HDMI_D0-
- C205 pad 2: GND -> /FPGA/_HDMI_D0-
- C206 pad 1: /#3.3V -> /FPGA/HDMI_D0+
- C206 pad 2: GND -> /FPGA/_HDMI_D0+
- C207 pad 1: /#3.3V -> /FPGA/HDMI_CK-
- C207 pad 2: GND -> /FPGA/_HDMI_CK-
- C208 pad 1: /#3.3V -> /FPGA/HDMI_CK+
- C208 pad 2: GND -> /FPGA/_HDMI_CK+
- C301 pad 1: /#2.5V -> /FPGA/2.5V
- C302 pad 1: /#2.5V -> /FPGA/2.5V
- C303 pad 1: /#2.5V -> /FPGA/2.5V
- C304 pad 1: /#2.5V -> /FPGA/2.5V
- C305 pad 1: /#1.1V -> /FPGA/1.1V
- C306 pad 1: /#1.1V -> /FPGA/1.1V
- C307 pad 1: /#1.1V -> /FPGA/1.1V
- C308 pad 1: /#1.1V -> /FPGA/1.1V
- C310 pad 1: /#1.1V -> /FPGA/1.1V
- C311 pad 1: /#1.1V -> /FPGA/1.1V
- C313 pad 1: /#3.3V -> /FPGA/3.3V
- C315 pad 1: /#3.3V -> /FPGA/3.3V
- C316 pad 1: /#3.3V -> /FPGA/3.3V
- C317 pad 1: /#3.3V -> /FPGA/3.3V
- C318 pad 1: /#3.3V -> /FPGA/3.3V
- C319 pad 1: /#3.3V -> /FPGA/3.3V
- C401 pad 1: /#3.3V -> /FPGA/3.3V
- C502 pad 1: /#3.3V -> /FPGA/3.3V
- C802 pad 1: /#3.3V -> /FPGA/3.3V
- C902 pad 1: /#3.3V -> /FPGA/3.3V
- J101 pad 13: /#3.3V -> /FPGA/3.3V
- J101 pad 14: /#3.3V -> /FPGA/3.3V
- J102 pad 1: /#3.3V -> /FPGA/3.3V
- J102 pad 11: /FPGA/FPGA_BANK6_IO4 -> /FPGA_BANK6_IO4
- J102 pad 12: /FPGA/FPGA_BANK6_IO5 -> /FPGA_BANK6_IO5
- J102 pad 13: /FPGA/FPGA_BANK6_IO2 -> /FPGA_BANK6_IO2
- J102 pad 14: /FPGA/FPGA_BANK6_IO3 -> /FPGA_BANK6_IO3
- J102 pad 15: /FPGA/FPGA_BANK6_IO0 -> /FPGA_BANK6_IO0
- J102 pad 16: /FPGA/FPGA_BANK6_IO1 -> /FPGA_BANK6_IO1
- J102 pad 19: /FPGA/FPGA_BANK7_IO10 -> /FPGA_BANK7_IO10
- J102 pad 20: /FPGA/FPGA_BANK7_IO11 -> /FPGA_BANK7_IO11
- J102 pad 21: /FPGA/FPGA_BANK7_IO8 -> /FPGA_BANK7_IO8
- J102 pad 22: /FPGA/FPGA_BANK7_IO9 -> /FPGA_BANK7_IO9
- J102 pad 23: /FPGA/FPGA_BANK7_IO6 -> /FPGA_BANK7_IO6
- J102 pad 24: /FPGA/FPGA_BANK7_IO7 -> /FPGA_BANK7_IO7
- J102 pad 25: /FPGA/FPGA_BANK7_IO4 -> /FPGA_BANK7_IO4
- J102 pad 26: /FPGA/FPGA_BANK7_IO5 -> /FPGA_BANK7_IO5
- J102 pad 27: /FPGA/FPGA_BANK7_IO2 -> /FPGA_BANK7_IO2
- J102 pad 28: /FPGA/FPGA_BANK7_IO3 -> /FPGA_BANK7_IO3
- J102 pad 29: /FPGA/FPGA_BANK7_IO0 -> /FPGA_BANK7_IO0
- J102 pad 3: /SPI5_MISO -> /EXT_SPI_MISO
- J102 pad 30: /FPGA/FPGA_BANK7_IO1 -> /FPGA_BANK7_IO1
- J102 pad 5: /SPI5_SCK -> /EXT_SPI_SCK
- J102 pad 7: /SPI5_MOSI -> /EXT_SPI_MOSI
- J102 pad 9: /SPI5_NSS -> /EXT_SPI_NSS
- J103 pad 11: /FPGA/FPGA_BANK0_IO8 -> /FPGA_BANK0_IO8
- J103 pad 12: /FPGA/FPGA_BANK0_IO9 -> /FPGA_BANK0_IO9
- J103 pad 13: /FPGA/FPGA_BANK0_IO6 -> /FPGA_BANK0_IO6
- J103 pad 14: /FPGA/FPGA_BANK0_IO7 -> /FPGA_BANK0_IO7
- J103 pad 15: /FPGA/FPGA_BANK0_IO4 -> /FPGA_BANK0_IO4
- J103 pad 16: /FPGA/FPGA_BANK0_IO5 -> /FPGA_BANK0_IO5
- J103 pad 17: /FPGA/FPGA_BANK0_IO2 -> /FPGA_BANK0_IO2
- J103 pad 18: /FPGA/FPGA_BANK0_IO3 -> /FPGA_BANK0_IO3
- J103 pad 19: /FPGA/FPGA_BANK0_IO0 -> /FPGA_BANK0_IO0
- J103 pad 20: /FPGA/FPGA_BANK0_IO1 -> /FPGA_BANK0_IO1
- J103 pad 21: /FPGA/FPGA_BANK1_IO14 -> /FPGA_BANK1_IO14
- J103 pad 22: /FPGA/FPGA_BANK1_IO15 -> /FPGA_BANK1_IO15
- J103 pad 23: /FPGA/FPGA_BANK1_IO12 -> /FPGA_BANK1_IO12
- J103 pad 24: /FPGA/FPGA_BANK1_IO13 -> /FPGA_BANK1_IO13
- J103 pad 25: /FPGA/FPGA_BANK1_IO10 -> /FPGA_BANK1_IO10
- J103 pad 26: /FPGA/FPGA_BANK1_IO11 -> /FPGA_BANK1_IO11
- J103 pad 27: /FPGA/FPGA_BANK1_IO8 -> /FPGA_BANK1_IO8
- J103 pad 28: /FPGA/FPGA_BANK1_IO9 -> /FPGA_BANK1_IO9
- J103 pad 29: /FPGA/FPGA_BANK1_IO6 -> /FPGA_BANK1_IO6
- J103 pad 30: /FPGA/FPGA_BANK1_IO7 -> /FPGA_BANK1_IO7
- J103 pad 31: /FPGA/FPGA_BANK1_IO4 -> /FPGA_BANK1_IO4
- J103 pad 32: /FPGA/FPGA_BANK1_IO5 -> /FPGA_BANK1_IO5
- J103 pad 33: /FPGA/FPGA_BANK1_IO2 -> /FPGA_BANK1_IO2
- J103 pad 34: /FPGA/FPGA_BANK1_IO3 -> /FPGA_BANK1_IO3
- J103 pad 35: /FPGA/FPGA_BANK1_IO0 -> /FPGA_BANK1_IO0
- J103 pad 36: /FPGA/FPGA_BANK1_IO1 -> /FPGA_BANK1_IO1
- J103 pad 5: /#3.3V -> /FPGA/3.3V
- J103 pad 6: /#3.3V -> /FPGA/3.3V
- J201 pad 1: unconnected-(J201-Pin_1-Pad1) -> /FPGA/_HDMI_D2+
- J201 pad 10: unconnected-(J201-Pin_10-Pad10) -> /FPGA/_HDMI_CK+
- J201 pad 12: Net-(J201-Pin_12) -> /FPGA/_HDMI_CK-
- J201 pad 13: /MCU/VCP_RX -> unconnected-(J201-CEC-Pad13)
- J201 pad 14: /MCU/VCP_TX -> unconnected-(J201-UTILITY-Pad14)
- J201 pad 2: unconnected-(J201-Pin_2-Pad2) -> GND
- J201 pad 3: /#3.3V -> /FPGA/_HDMI_D2-
- J201 pad 4: Net-(J201-Pin_4) -> /FPGA/_HDMI_D1+
- J201 pad 6: Net-(J201-Pin_6) -> /FPGA/_HDMI_D1-
- J201 pad 7: GND -> /FPGA/_HDMI_D0+
- J201 pad 8: unconnected-(J201-Pin_8-Pad8) -> GND
- J201 pad 9: unconnected-(J201-Pin_9-Pad9) -> /FPGA/_HDMI_D0-
- J202 pad 1: /MCU/SDMMC_D2 -> /FPGA/SDMMC_D2
- J202 pad 10: /#3.3V -> /FPGA/3.3V
- J202 pad 2: /MCU/SDMMC_D3 -> /FPGA/SDMMC_D3
- J202 pad 3: /MCU/SDMMC_CMD -> /FPGA/SDMMC_CMD
- J202 pad 4: /#3.3V -> /FPGA/3.3V
- J202 pad 5: /MCU/SDMMC_CLK -> /FPGA/SDMMC_CLK
- J202 pad 7: /MCU/SDMMC_D0 -> /FPGA/SDMMC_D0
- J202 pad 8: /MCU/SDMMC_D1 -> /FPGA/SDMMC_D1
- J202 pad 9: /MCU/CARD_DETECT -> /FPGA/CARD_DETECT
- J203 pad 5: /MCU/USB_D- -> /USB/USB_D-
- J203 pad 6: /MCU/USB_D+ -> /USB/USB_D+
- J203 pad 7: /MCU/USB_D+ -> /USB/USB_D+
- J203 pad 8: /MCU/USB_D- -> /USB/USB_D-
- JP101 pad 1: /#3.3V -> /FPGA/3.3V
- JP102 pad 1: /#3.3V -> /FPGA/3.3V
- JP103 pad 1: /#3.3V -> /FPGA/3.3V
- R101 pad 1: /#3.3V -> /FPGA/3.3V
- R201 pad 1: /#3.3V -> /FPGA/3.3V
- R201 pad 2: /MCU/USER_BP1 -> Net-(U10-~{WP})
- R202 pad 1: GND -> /FPGA/3.3V
- R202 pad 2: /MCU/CARD_DETECT -> Net-(U10-~{HOLD})
- R203 pad 1: Net-(J201-Pin_4) -> /FPGA/3.3V
- R203 pad 2: /MCU/SWDIO -> Net-(U203I-DONE)
- R204 pad 1: Net-(J201-Pin_6) -> /FPGA/3.3V
- R204 pad 2: /MCU/SWCLK -> /FPGA/~{INIT}
- R205 pad 1: Net-(J201-Pin_12) -> /FPGA/3.3V
- R205 pad 2: /MCU/RESET -> /FPGA/~{PROGRAM}
- R213 pad 1: /MCU/VBUS_SENSE -> /USB/VBUS_SENSE
- R301 pad 1: /#3.3V -> /FPGA/3.3V
- R301 pad 2: Net-(U301H-TDO) -> /FPGA/JTAG.TDO
- R302 pad 2: Net-(U301H-TCK) -> /FPGA/JTAG.TCK
- R303 pad 1: /#3.3V -> /FPGA/3.3V
- R303 pad 2: Net-(U301H-TDI) -> /FPGA/JTAG.TDI
- R304 pad 1: /#3.3V -> /FPGA/3.3V
- R304 pad 2: Net-(U301H-TMS) -> /FPGA/JTAG.TMS
- R308 pad 1: /#3.3V -> /FPGA/3.3V
- R309 pad 1: /#3.3V -> /FPGA/3.3V
- R401 pad 1: /#3.3V -> /FPGA/3.3V
- R501 pad 2: /#3.3V -> /FPGA/3.3V
- R503 pad 1: /#3.3V -> /FPGA/3.3V
- R801 pad 2: /#1.1V -> /FPGA/1.1V
- R803 pad 1: /#1.1V -> /FPGA/1.1V
- R901 pad 2: /#2.5V -> /FPGA/2.5V
- R903 pad 1: /#2.5V -> /FPGA/2.5V
- SW201 pad 1: /MCU/USER_BP1 -> Net-(R1206-Pad2)
- U1001 pad 4: /#3.3V -> /FPGA/3.3V
- U1001 pad 5: /I2C1_SCL -> /JTAG/PSU.SCL
- U1001 pad 6: /I2C1_SDA -> /JTAG/PSU.SDA
- U1001 pad 7: /I2C1_SCL -> /JTAG/PSU.SCL
- U202 pad 2: /MCU/USB_D- -> /USB/USB_D-
- U202 pad 3: /MCU/USB_D+ -> /USB/USB_D+
- U202 pad 6: /MCU/USB_D+ -> /USB/USB_D+
- U202 pad 7: /MCU/USB_D- -> /USB/USB_D-
- U401 pad 1: /#3.3V -> /FPGA/3.3V
- U401 pad 3: /#3.3V -> /FPGA/3.3V
- U501 pad 4: /#3.3V -> /FPGA/3.3V
- U501 pad 5: /I2C1_SCL -> /JTAG/PSU.SCL
- U501 pad 6: /I2C1_SDA -> /JTAG/PSU.SDA
- U801 pad 4: /#3.3V -> /FPGA/3.3V
- U801 pad 5: /I2C1_SCL -> /JTAG/PSU.SCL
- U801 pad 6: /I2C1_SDA -> /JTAG/PSU.SDA
- U801 pad 7: /#3.3V -> /FPGA/3.3V
- U901 pad 4: /#3.3V -> /FPGA/3.3V
- U901 pad 5: /I2C1_SCL -> /JTAG/PSU.SCL
- U901 pad 6: /I2C1_SDA -> /JTAG/PSU.SDA
- U901 pad 7: /I2C1_SDA -> /JTAG/PSU.SDA
- X1 pad 1: /#3.3V -> /FPGA/3.3V
- X1 pad 3: /FPGA/FPGA_OPT_CLK -> /FPGA/FPGA_CLK
- X1 pad 4: /#3.3V -> /FPGA/3.3V
- Y201 pad 1: Net-(U203-PH0) -> Net-(U1201-XIN)
- Y201 pad 3: Net-(U203-PH1) -> Net-(U1201-XOUT)
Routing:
- net /#1.1V: track 130.5 -> 0.00 mm, vias 7 -> 0
- net /JTAG/PSU.SCL: track 0.00 -> 113.1 mm, vias 0 -> 6
- net /#3.3V: track 110.7 -> 0.00 mm, vias 44 -> 0
- net /JTAG/PSU.SDA: track 0.00 -> 108.9 mm, vias 0 -> 6
- net /I2C1_SCL: track 128.5 -> 25.8 mm, vias 5 -> 1
- net /I2C1_SDA: track 128.2 -> 26.8 mm, vias 5 -> 1
- net /#2.5V: track 97.8 -> 0.00 mm, vias 5 -> 0
- net /FPGA/3.3V: track 0.00 -> 84.4 mm, vias 0 -> 47
- net /MCU/VCap: track 61.9 -> 0.00 mm, vias 5 -> 0
- net /FPGA/FPGA_UART2_TX: track 57.2 -> 0.00 mm, vias 2 -> 0
- net /FPGA/FPGA_UART2_RX: track 55.4 -> 0.00 mm, vias 2 -> 0
- net /SPI5_MOSI: track 53.5 -> 0.00 mm, vias 1 -> 0
- net /FPGA/FPGA_UART_TX: track 52.7 -> 0.00 mm, vias 2 -> 0
- net /FPGA/FPGA_UART_RX: track 52.6 -> 0.00 mm, vias 2 -> 0
- net /FPGA_BANK1_IO1: track 0.00 -> 52.0 mm
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- added copper zone on In2.Cu, net /FPGA/3.3V
- added copper zone on In2.Cu, net GND
- removed copper zone on In2.Cu, net /#3.3V
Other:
- board text added: "ER"
- board text added: "Fusion 3.0 LPP (2025)"
- board text added: "JTAG & Debug"
- board text added: "RP Boot"
- board text added: "RP Reset"
- board text added: "RX"
- board text added: "TX"
- board text added: "USB2.0"
- board text removed: "BOOT0"
- board text removed: "BP1"
- board text removed: "BP2"
- board text removed: "CFG0"
- board text removed: "CFG1"
- board text removed: "CFG2"
- board text removed: "Fusion 2.0 LPP (2025)"
- board text removed: "LED1"
- board text removed: "LED2"
- board text removed: "RESET"
